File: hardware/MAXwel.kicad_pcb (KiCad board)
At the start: 2 copper layers, 78.7 x 85.7 mm, 155 parts, among them J1 Conn_02x05_Odd_Even, J2 Conn_02x12_Counter_Clockwise, J3 Barrel_Jack_Switch_Pin3Ring, SW1 SW_Push_Dual, SW10 SW_Wuerth_450301014042, SW11 SW_Wuerth_450301014042, SW12 SW_Wuerth_450301014042, SW13 SW_Wuerth_450301014042, SW2 SW_Push_Dual, SW3 SW_Push_Dual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

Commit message: update sw_slide footprint, added part references and QR code on backside
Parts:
- added G***: LOGO, Library:qr_code, B.Cu at (139.7, 71.9)
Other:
- board text added: "MAXwel FPGA Board"
- board text removed: "MAXwel FPGA Board Michael Hohenstein"

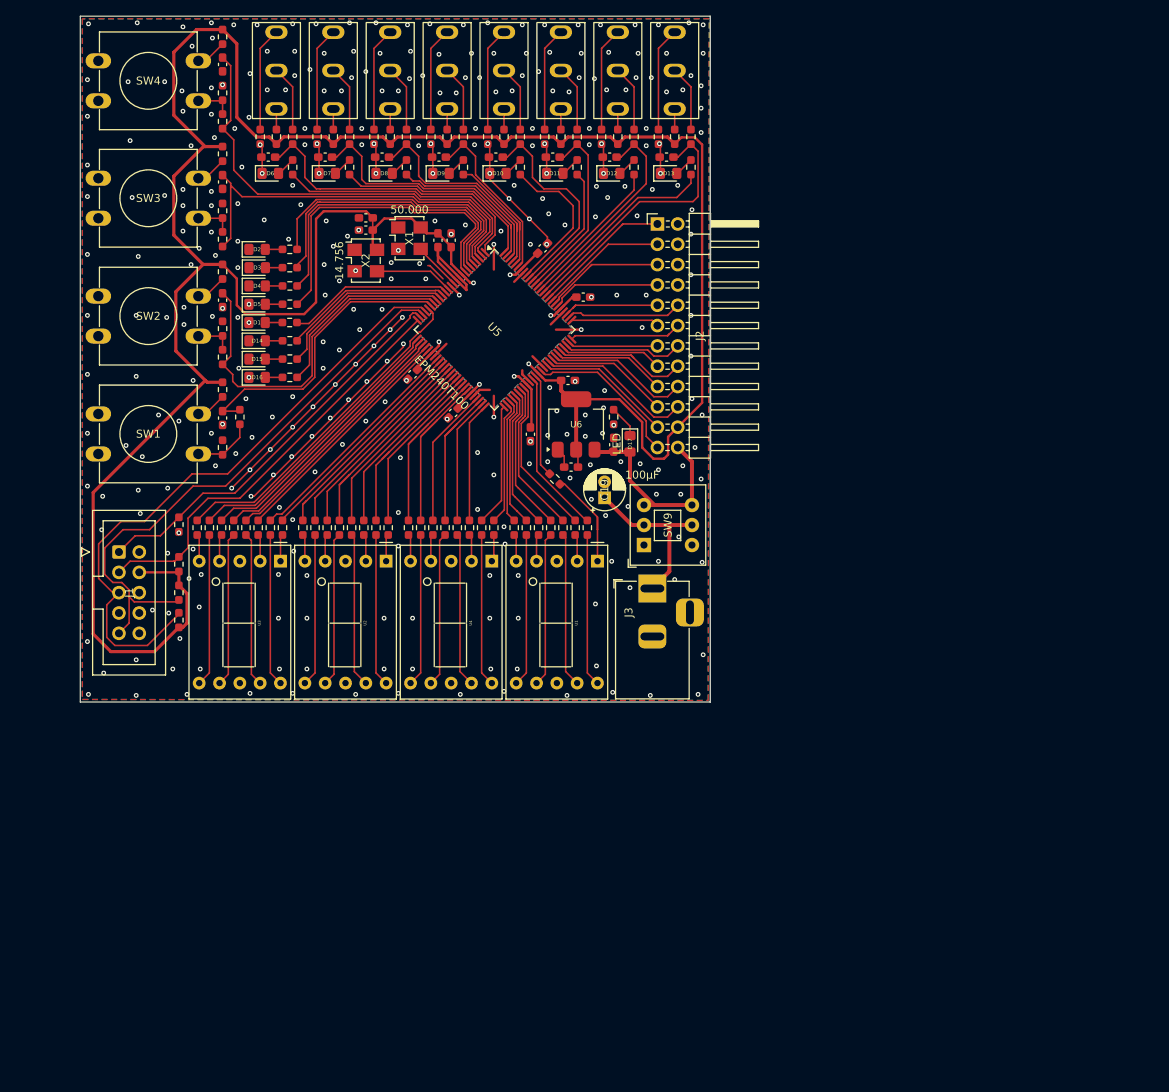
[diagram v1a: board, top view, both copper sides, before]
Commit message: update pin mapping to match new design
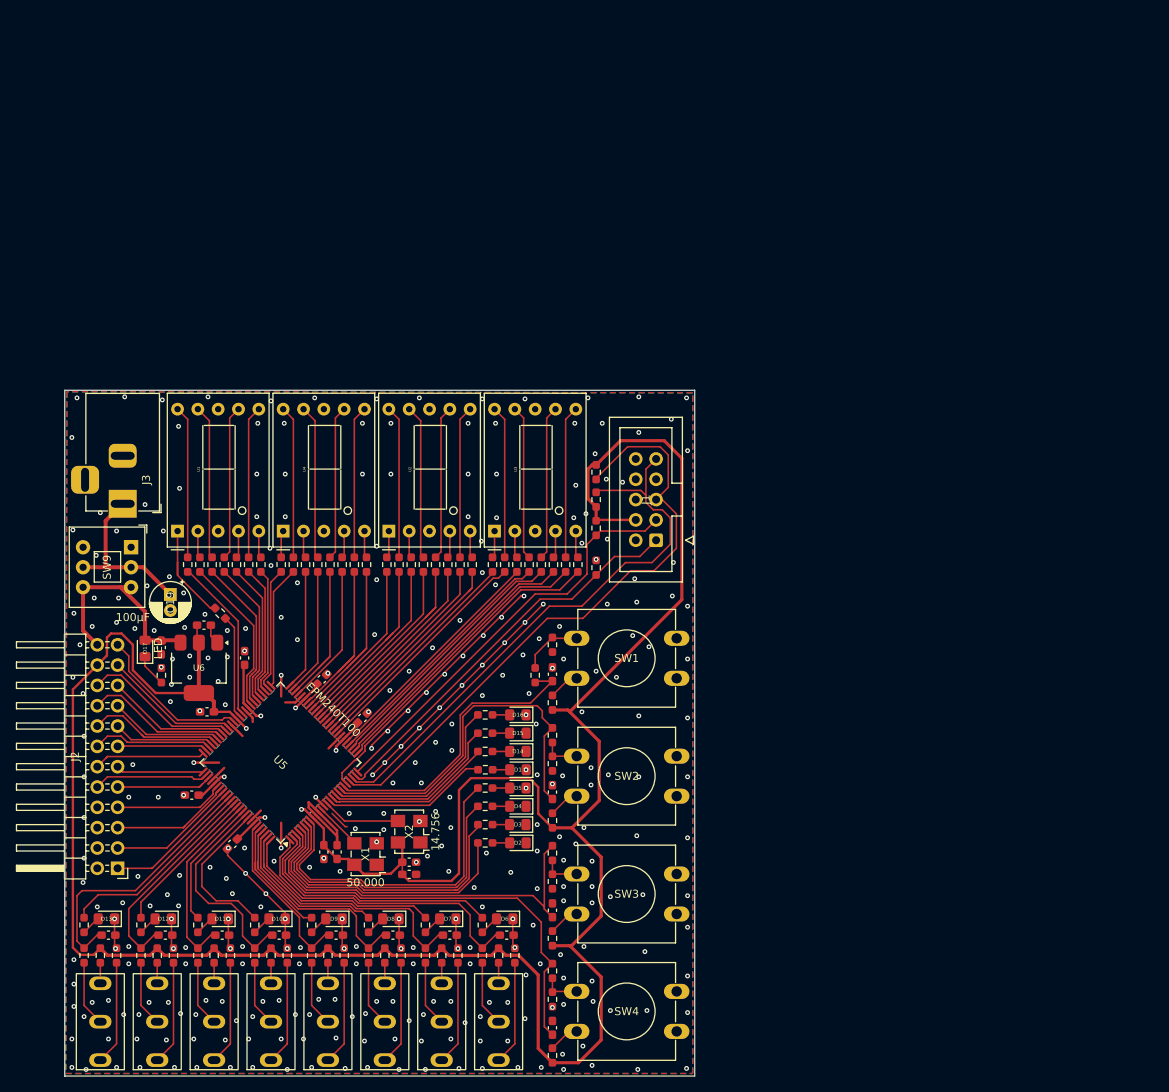
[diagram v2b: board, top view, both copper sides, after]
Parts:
- moved SW6 138.9 mm to (110.1, 146.5), turned to 90 degrees
- moved R61 133.8 mm to (166.6, 150.7), turned to -90 degrees
- moved SW7 132.1 mm to (117.2, 146.5), turned to 90 degrees
- moved R68 127.4 mm to (108.0, 138.2), turned to -90 degrees
- moved C14 127.3 mm to (166.6, 147.2), turned to 90 degrees
- moved SW10 126.5 mm to (124.3, 146.5), turned to 90 degrees
- moved R71 125.0 mm to (110.1, 138.2), turned to 90 degrees
- moved R72 122.7 mm to (112.1, 138.2), turned to 90 degrees
- moved SW11 122.4 mm to (131.4, 146.5), turned to 90 degrees
- moved SW5 122.1 mm to (159.9, 146.5), turned to 90 degrees
- moved R59 121.3 mm to (108.0, 134.4), turned to -90 degrees
- moved SW4 121.0 mm to (169.6, 142.7), turned to 0 degrees
- moved R51 120.6 mm to (166.6, 143.7), turned to 90 degrees
- moved SW13 119.8 mm to (138.5, 146.5), turned to 90 degrees
- moved C16 119.7 mm to (111.1, 135.6), turned to 0 degrees
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
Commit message: removed resistors at sliding switches, 5mm smaller circuit board
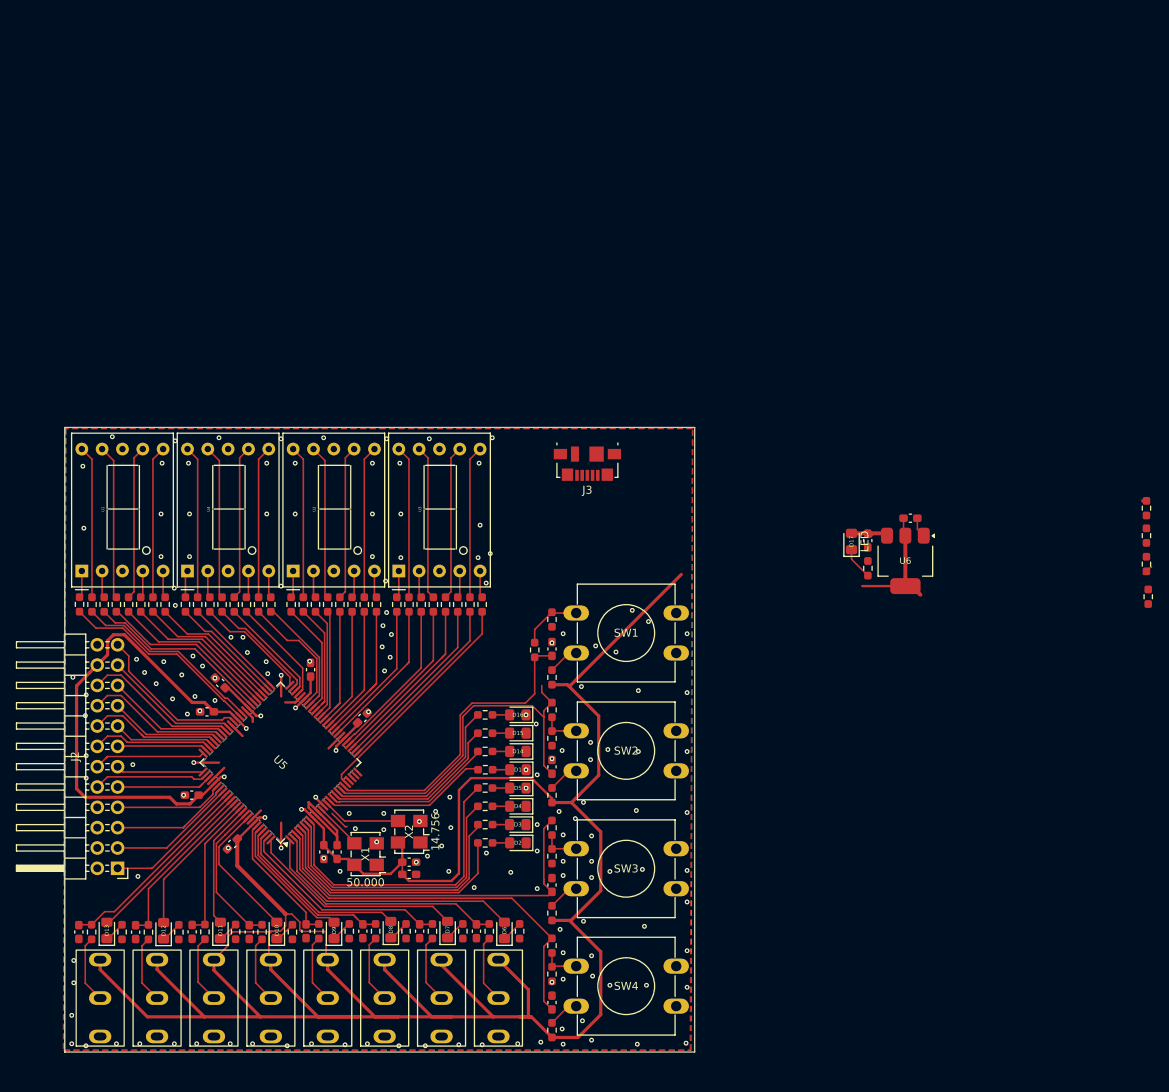
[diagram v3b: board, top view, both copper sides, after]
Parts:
- removed C19: 100µF, Capacitor_THT:CP_Radial_D5.0mm_P2.00mm
- removed J1: Conn_02x05_Odd_Even, Connector_IDC:IDC-Header_2x05_P2.54mm_Vertical
- removed R66, R67, R71, R72, R73, R74, R75, R76, R82, R83, R84, R85, R86, R87, R88, R89: 10K, Resistor_SMD:R_0603_1608Metric_Pad0.98x0.95mm_HandSolder
- removed SW9: SW_Push_DPDT, Button_Switch_THT:SW_Push_2P2T_Toggle_CK_PVA2OAH5xxxxxxV2
- J3: value Barrel_Jack_Switch_Pin3Ring -> USB_B_Micro; footprint Connector_BarrelJack:BarrelJack_Horizontal -> Connector_USB:USB_Micro-B_Molex_47346-0001
- R64, R68, R69, R70, R78, R79, R80, R81: value 1K -> 10K
- moved C24 89.3 mm to (206.0, 86.3)
- moved C25 89.3 mm to (211.3, 83.5)
- moved R77 89.3 mm to (206.0, 89.8)
- moved D17 89.3 mm to (204.0, 86.4)
- moved U6 89.3 mm to (210.7, 88.8)
- moved R33 69.1 mm to (241.1, 93.3)
- moved R30 68.9 mm to (240.8, 82.3)
- moved R31 68.9 mm to (240.8, 85.7)
- moved R32 68.9 mm to (240.8, 89.2)
- moved J3 58.3 mm to (170.9, 76.7), turned to 180 degrees
- moved R13 17.6 mm to (107.5, 94.3), turned to -90 degrees
- moved R34 13.0 mm to (131.4, 94.3)
- moved R37 13.0 mm to (126.8, 94.3)
- moved R38 13.0 mm to (125.3, 94.3)
- moved R39 13.0 mm to (123.8, 94.3)
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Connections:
- C24 pad 1: +5V -> Net-(D17-A)
- D10 pad 1: GND -> Net-(D10-K)
- D11 pad 1: GND -> Net-(D11-K)
- D12 pad 1: GND -> Net-(D12-K)
- D13 pad 1: GND -> Net-(D13-K)
- D17 pad 2: +5V -> Net-(D17-A)
- D6 pad 1: GND -> Net-(D6-K)
- D7 pad 1: GND -> Net-(D7-K)
- D8 pad 1: GND -> Net-(D8-K)
- D9 pad 1: GND -> Net-(D9-K)
- J3 pad 1: Net-(C19-Pad1) -> Net-(D17-A)
- J3 pad 2: GND -> unconnected-(J3-D--Pad2)
- J3 pad 3: GND -> unconnected-(J3-D+-Pad3)
- R52 pad 1: Net-(U5-IO1_2) -> Net-(D6-K)
- R52 pad 2: Net-(D6-A) -> GND
- R53 pad 1: Net-(U5-IO2_100) -> Net-(D7-K)
- R53 pad 2: Net-(D7-A) -> GND
- R54 pad 1: Net-(U5-IO2_98) -> Net-(D8-K)
- R54 pad 2: Net-(D8-A) -> GND
- R55 pad 1: Net-(U5-IO2_96) -> Net-(D9-K)
- R55 pad 2: Net-(D9-A) -> GND
- R56 pad 1: Net-(U5-IO2_92) -> Net-(D10-K)
- R56 pad 2: Net-(D10-A) -> GND
- R57 pad 1: Net-(U5-IO2_90) -> Net-(D11-K)
- R57 pad 2: Net-(D11-A) -> GND
- R58 pad 1: Net-(U5-IO2_88) -> Net-(D12-K)
- R58 pad 2: Net-(D12-A) -> GND
- R59 pad 1: Net-(U5-IO2_86) -> Net-(D13-K)
- R59 pad 2: Net-(D13-A) -> GND
- SW10 pad 2: Net-(SW10-C) -> GND
- SW10 pad 3: Net-(SW10-A) -> +3V3
- SW11 pad 2: Net-(SW11-C) -> GND
- SW11 pad 3: Net-(SW11-A) -> +3V3
- SW12 pad 2: Net-(SW12-C) -> GND
- SW12 pad 3: Net-(SW12-A) -> +3V3
- SW13 pad 2: Net-(SW13-C) -> GND
- SW13 pad 3: Net-(SW13-A) -> +3V3
- SW5 pad 2: Net-(SW5-C) -> GND
- SW5 pad 3: Net-(SW5-A) -> +3V3
- SW6 pad 2: Net-(SW6-C) -> GND
- SW6 pad 3: Net-(SW6-A) -> +3V3
- SW7 pad 2: Net-(SW7-C) -> GND
- SW7 pad 3: Net-(SW7-A) -> +3V3
- SW8 pad 2: Net-(SW8-C) -> GND
- SW8 pad 3: Net-(SW8-A) -> +3V3
- U5 pad 100: Net-(U5-IO2_100) -> Net-(D7-A)
- U5 pad 2: Net-(U5-IO1_2) -> Net-(D6-A)
- U5 pad 86: Net-(U5-IO2_86) -> Net-(D13-A)
- U5 pad 88: Net-(U5-IO2_88) -> Net-(D12-A)
- U5 pad 90: Net-(U5-IO2_90) -> Net-(D11-A)
- U5 pad 92: Net-(U5-IO2_92) -> Net-(D10-A)
- U5 pad 96: Net-(U5-IO2_96) -> Net-(D9-A)
- U5 pad 98: Net-(U5-IO2_98) -> Net-(D8-A)
- U6 pad 3: +5V -> Net-(D17-A)
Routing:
- net GND: track 141.7 -> 40.0 mm, vias 344 -> 170
- net Net-(U5-TMS): track 78.4 -> 0.15 mm
- net Net-(U5-TDI): track 72.0 -> 0.34 mm
- net +3V3: track 361.8 -> 418.3 mm
- net Net-(U5-TDO): track 52.9 -> 1.14 mm
- net Net-(U5-TCK): track 50.4 -> 0.00 mm
- net Net-(U5-IO1_2): track 32.8 -> 0.00 mm
- net Net-(D6-A): track 2.46 -> 33.1 mm
- net +5V: track 27.3 -> 0.21 mm
- net Net-(U5-IO2_100): track 26.0 -> 0.00 mm
- net Net-(U5-IO2_86): track 25.1 -> 0.00 mm
- net Net-(D7-A): track 2.46 -> 27.2 mm
- net Net-(C19-Pad1): track 21.1 -> 0.00 mm
- net Net-(U5-IO2_98): track 20.5 -> 0.00 mm
- net Net-(D8-A): track 2.46 -> 22.5 mm
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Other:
- board size 78.7 x 85.7 mm -> 78.7 x 78.1 mm

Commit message: tighter layout
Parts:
- moved D2 2.88 mm to (160.6, 126.4)
- moved D3 2.88 mm to (160.6, 124.2)
- moved R2 2.88 mm to (156.5, 126.4)
- moved R3 2.88 mm to (156.5, 124.2)
- moved D1 2.88 mm to (160.6, 117.3)
- moved D4 2.88 mm to (160.6, 121.9)
- moved D5 2.88 mm to (160.6, 119.6)
- moved R1 2.88 mm to (156.5, 117.3)
- moved R4 2.88 mm to (156.5, 121.9)
- moved R5 2.88 mm to (156.5, 119.6)
- moved D14 2.88 mm to (160.6, 115.0)
- moved D15 2.88 mm to (160.6, 112.7)
- moved D16 2.88 mm to (160.6, 110.4)
- moved R62 2.88 mm to (156.5, 115.0)
- moved R63 2.88 mm to (156.5, 112.7)
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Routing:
- net +3V3: track 418.3 -> 408.0 mm
- net Net-(U5-IO1_8): track 37.8 -> 30.5 mm
- net Net-(U5-IO1_7): track 36.1 -> 28.9 mm
- net Net-(U5-IO1_6): track 34.5 -> 27.7 mm
- net Net-(U5-IO1_5): track 32.8 -> 26.0 mm
- net GND: track 40.0 -> 43.2 mm, vias 170 -> 172
- net Net-(U5-IO1_4): track 47.6 -> 44.9 mm
- net Net-(U5-IO1_15): track 20.8 -> 18.1 mm
- net Net-(U5-IO1_20): track 38.6 -> 41.0 mm
- net Net-(U5-IO1_17): track 23.0 -> 21.0 mm
- net Net-(U5-IO2_95): track 16.9 -> 15.0 mm
- net Net-(U5-IO2_91): track 18.7 -> 16.7 mm
- net Net-(D12-A): track 18.4 -> 16.4 mm
- net Net-(U5-IO2_87): track 21.3 -> 19.3 mm
- net Net-(U5-IO2_89): track 17.9 -> 16.0 mm
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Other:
- board size 78.7 x 78.1 mm -> 77.4 x 76.1 mm
